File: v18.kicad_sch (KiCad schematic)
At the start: 59 parts, among them U51 ADP5071ACPZ, U52 TPS7A4700xRGW, U53 TPS7A3301RGW

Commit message: Whew.  DACs routed
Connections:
- net +20V: now also TP51.1
- net -20V: now also TP53.1
- net R18in: no longer TP51.1
- net RM18Vin: no longer TP53.1
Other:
- moved on the sheet: C523, C524, C525, C526, C527, C528, C529, C530, C543, C544, C545, C546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

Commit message: Tweaks following spice simulation.
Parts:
- added C551: 10u, Capacitor_SMD:C_0805_2012Metric, symbol Device:C
- added D55, D56: 1N5819WS, Diode_SMD:D_SOD-323, symbol Parts:1N5819WS
- added L56: 600, Inductor_SMD:L_0603_1608Metric, symbol Parts:L_Ferrite_Power
- L54, L55: value 100 -> 600; LCSC C14709 -> C1002
- renumbered C542 to C541, C543 to C542, C544 to C543, C545 to C544, C546 to C545, C547 to C546, C548 to C547, C549 to C548, C550 to C549, C551 to C550
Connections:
- net +18V: now also D55.1 (K)
- net -18V: now also C551.2, D56.2 (A), L56.2; no longer C544.2, C545.2, C546.2, C547.2, C548.2, C549.2, R541.1, TP54.1, U53.1 (OUT), U53.20 (OUT)
- net GNDPWR: now also C551.1, D55.2 (A), D56.1 (K)
- new net: C544.2, C545.2, C546.2, C547.2, C548.2, C549.2, L56.1, R541.1, TP54.1, U53.1 (OUT), U53.20 (OUT)
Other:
- moved on the sheet: C550

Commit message: About to delete scan...
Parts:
- C502: LCSC (none) -> C1588; now in the parts list
- D51, D52: Stock (none) -> 10
- L51, L52: Stock (none) -> 5
- R504: Stock (none) -> 50
- R513: Stock (none) -> 30
- TP51, TP52, TP53, TP54: Stock (none) -> -
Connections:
- net FB1: no longer names the net of R502.1, R503.2, R504.1, U51.5 (FB1)
- net FB2: no longer names the net of R512.2, R513.2, R514.1, U51.11 (FB2)
- net R18in: no longer names the net of C522.2, C523.2, R524.1, U52.13 (EN), U52.15 (IN), U52.16 (IN)
- net RM18Vin: no longer names the net of C541.1, C542.1, R544.1, U53.13 (EN), U53.15 (IN), U53.16 (IN)
- net Sn: no longer names the net of D52.1 (K), L52.1, U51.18 (SW2)
- net Sp: no longer names the net of D51.2 (A), L51.2, U51.20 (SW1)

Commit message: Scan deleted.
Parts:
- removed D53, D54: 1N5819WS, Diode_SMD:D_SOD-323, symbol Parts:1N5819WS
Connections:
- net at L54.2: now also R524.2
- net at L55.2: now also R544.2
- net +20V: no longer names the net of C504.2, C505.1, D51.1 (K), L54.1, R503.1, TP51.1
- net -20V: no longer names the net of C506.1, C508.2, D52.2 (A), L55.1, R514.2, TP53.1
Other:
- moved on the sheet: C522, C523, C524, C525, C526, C527, C528, C529, C530, C541, C542, C543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

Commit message: Most blocks there....
About to restore scan.
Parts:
- removed C550: 10u, Capacitor_SMD:C_0805_2012Metric, symbol Device:C
- removed R544: 1, Resistor_SMD:R_0603_1608Metric, symbol Device:R
- renumbered C507 to C50, C501 to C51, C504 to C52, C506 to C53
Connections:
- net -18V: now also C544.1, C545.1, C546.1, C547.1, C548.1, C549.1, R541.1, TP54.1, U53.1 (OUT), U53.20 (OUT); no longer C551.2, L56.2
- net GNDPWR: now also C52.2, C522.2, C523.2, C53.1, C543.2, C544.2, C546.2, C547.2, C548.2, C549.2, C551.2; no longer C52.1, C522.1, C523.1, C53.2, C543.1, C544.1, C546.1, C547.1, C548.1, C549.1, C551.1
- net at C505.1, D51.1 (K), L54.1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: now also C52.1; no longer C52.2
- net at C508.2, D52.2 (A), L55.1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: now also C53.2; no longer C53.1
- net i18: now reaches R524.1, U52.13 (EN), U52.15 (IN), U52.16 (IN)
- net i18: now also C522.1, C523.1; no longer C522.2, C523.2
- net at R541.2, R542.1, R543.1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: now also C545.2; no longer C545.1
- net im18: now reaches C541.1, C542.1, U53.13 (EN), U53.15 (IN), U53.16 (IN)
- net im18: now also L56.2
- net at L55.2: now also C551.1, L56.1
- net at U53.14 (NR/SS): now also C543.1; no longer C543.2
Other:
- moved on the sheet: C508, C52, C522, C523, C524, C525, C526, C527, C528, C529, C53, C530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

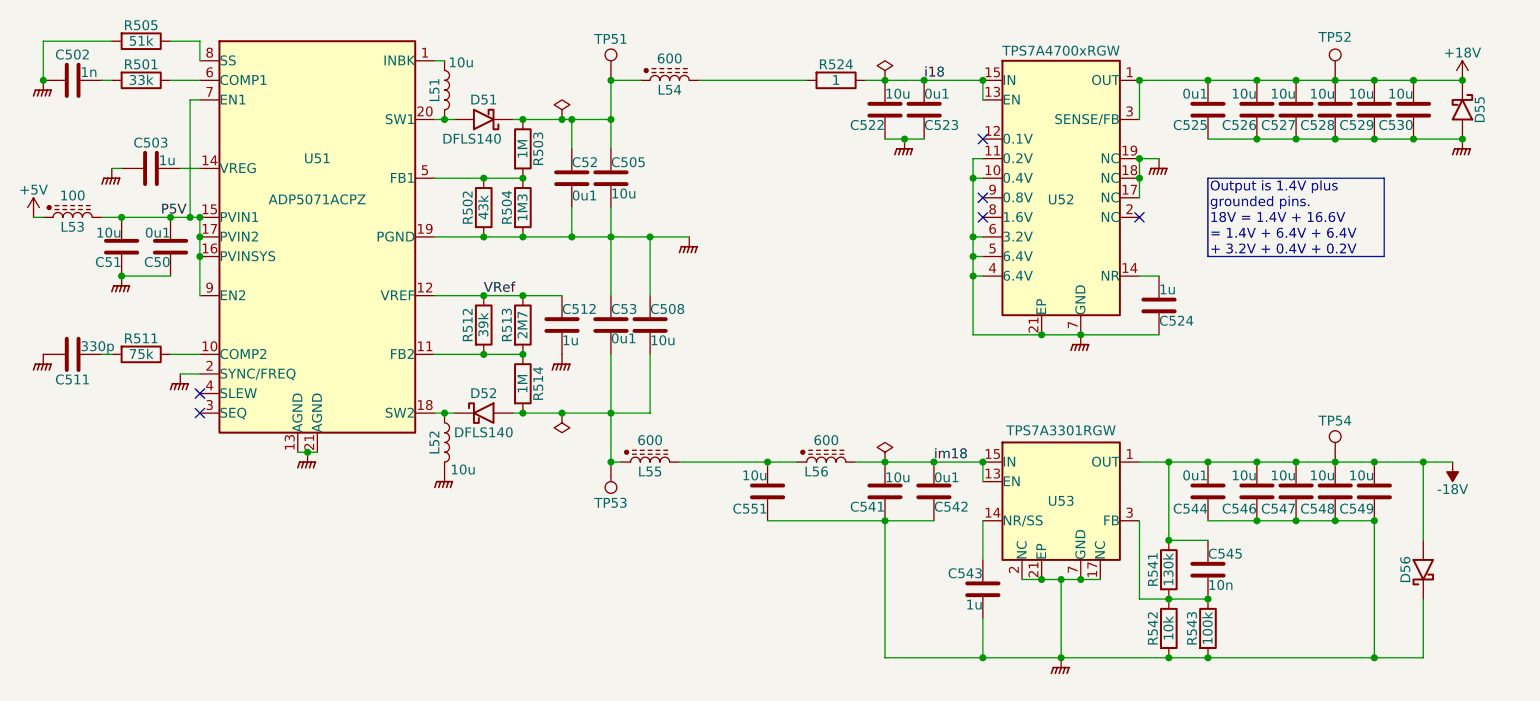
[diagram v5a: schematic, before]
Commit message: S&H restored.  Now to touch up connections etc.
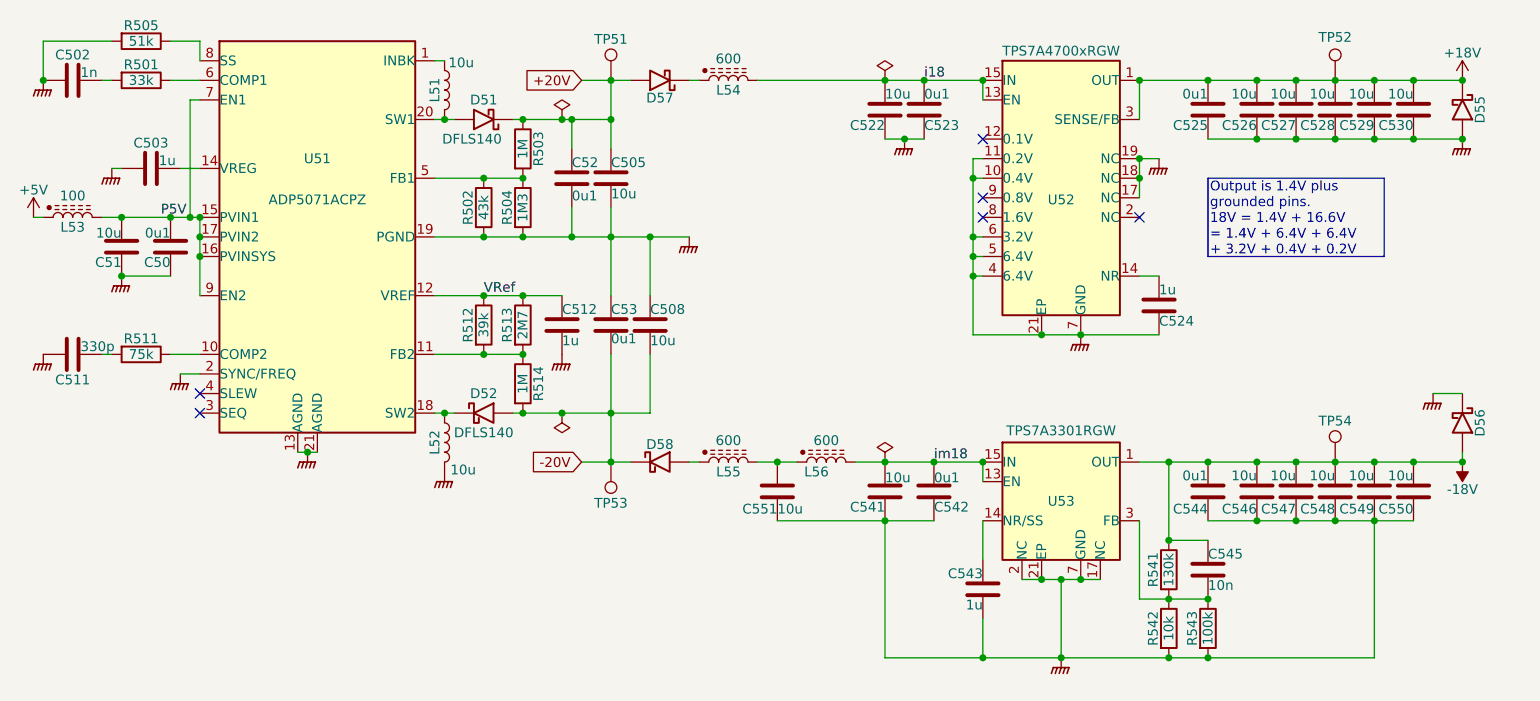
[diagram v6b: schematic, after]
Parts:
- removed R524: 1, Resistor_SMD:R_0603_1608Metric, symbol Device:R
- added C550: 10u, Capacitor_SMD:C_0805_2012Metric, symbol Device:C
- added D57, D58: 1N5819WS, Diode_SMD:D_SOD-323, symbol Parts:1N5819WS
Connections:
- net -18V: now also C550.1
- net GNDPWR: now also C550.2
- net i18: now also L54.2
- net +20V: now reaches C505.1, C52.1, D51.1 (K), R503.1, TP51.1
- net +20V: now also D57.2 (A); no longer L54.1
- net -20V: now reaches C508.2, C53.2, D52.2 (A), R514.2, TP53.1
- net -20V: now also D58.1 (K); no longer L55.1
- new net: D57.1 (K), L54.1
- new net: D58.2 (A), L55.1
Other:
- moved on the sheet: C551, D56, L54, L55

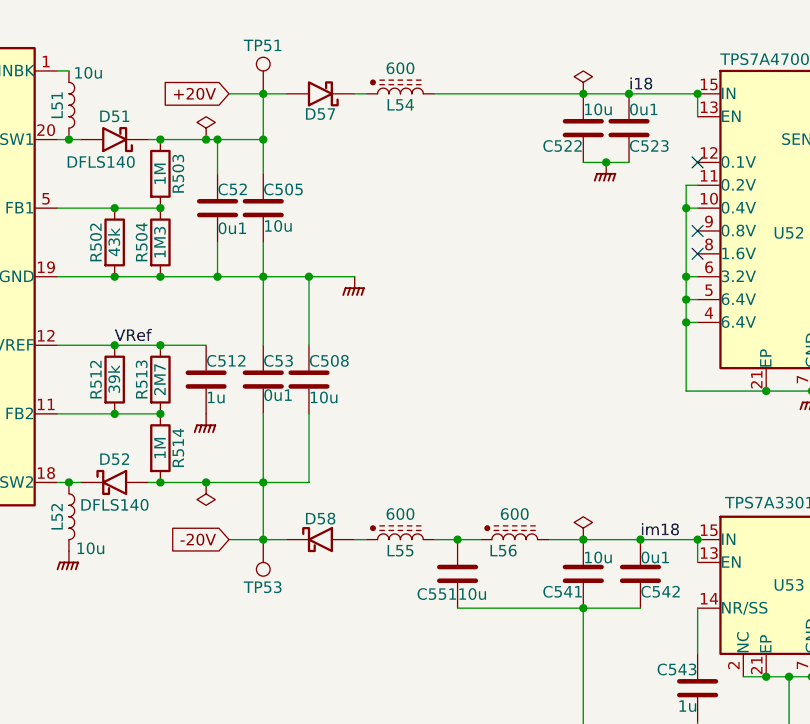
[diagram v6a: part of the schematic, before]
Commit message: Put ref filtering into the schematic.
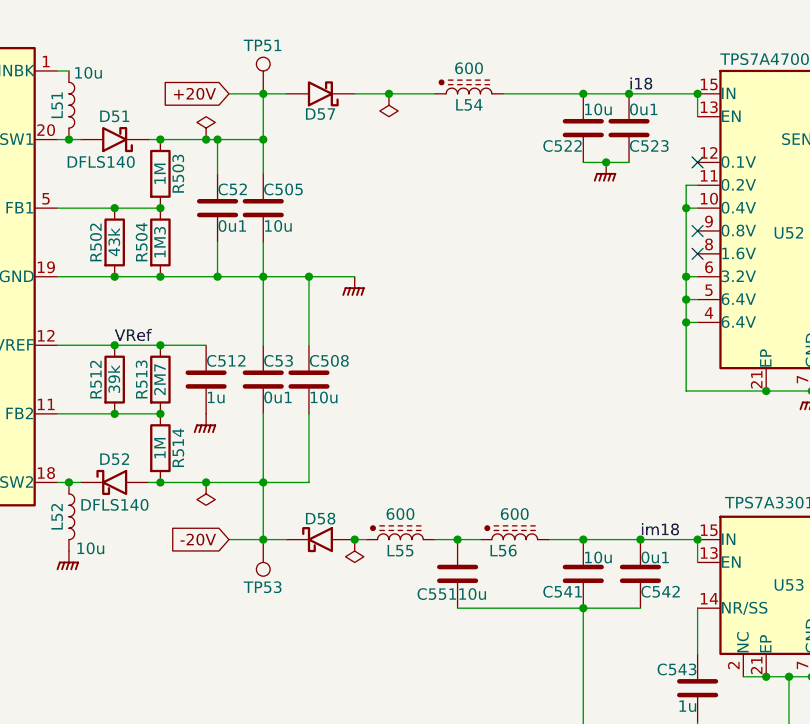
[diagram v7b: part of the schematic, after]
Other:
- moved on the sheet: L54
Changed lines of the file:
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@@
 	)
 	(junction
+		(at 144.78 92.71)
+		(diameter 0)
+		(color 0 0 0 0)
+	)
+	(junction
 		(at 245.11 50.8)
 		(diameter 0)
@@
 	)
 	(junction
+		(at 148.59 43.18)
+		(diameter 0)
+		(color 0 0 0 0)
+	)
+	(junction
 		(at 238.76 92.71)
 		(diameter 0)
@@
 	(wire
 		(pts
+			(xy 161.29 43.18) (xy 170.18 43.18)
+		)
+		(stroke
+			(width 0)
+			(type default)
+		)
+	)
+	(wire
+		(pts
 			(xy 134.62 52.07) (xy 134.62 48.26)
 		)
@@
 	(wire
 		(pts
-			(xy 144.78 43.18) (xy 146.05 43.18)
-		)
-		(stroke
-			(width 0)
-			(type default)
-		)
-	)
-	(wire
-		(pts
 			(xy 81.28 66.04) (xy 81.28 71.12)
 		)
@@
 	(wire
 		(pts
-			(xy 71.12 60.96) (xy 77.47 60.96)
+			(xy 144.78 43.18) (xy 148.59 43.18)
 		)
 		(stroke
@@
 	(wire
 		(pts
-			(xy 111.76 55.88) (xy 118.11 55.88)
+			(xy 71.12 60.96) (xy 77.47 60.96)
 		)
 		(stroke
@@
 	(wire
 		(pts
-			(xy 203.2 55.88) (xy 203.2 58.42)
+			(xy 111.76 55.88) (xy 118.11 55.88)
 		)
 		(stroke
@@
 	(wire
 		(pts
-			(xy 170.18 43.18) (xy 175.26 43.18)
+			(xy 203.2 55.88) (xy 203.2 58.42)
 		)
 		(stroke
@@
 	(wire
 		(pts
-			(xy 223.52 100.33) (xy 228.6 100.33)
+			(xy 170.18 43.18) (xy 175.26 43.18)
 		)
 		(stroke
@@
 	(wire
 		(pts
-			(xy 153.67 43.18) (xy 170.18 43.18)
+			(xy 223.52 100.33) (xy 228.6 100.33)
 		)
 		(stroke
@@
 	(wire
 		(pts
+			(xy 148.59 43.18) (xy 153.67 43.18)
+		)
+		(stroke
+			(width 0)
+			(type default)
+		)
+	)
+	(wire
+		(pts
 			(xy 144.78 92.71) (xy 146.05 92.71)
 		)
@@
 	(symbol
 		(lib_id "Parts:L_Ferrite_Power")
-		(at 149.86 43.18 90)
+		(at 157.48 43.18 90)
 		(unit 1)
 		(exclude_from_sim no)
@@
 		(dnp no)
 		(property "Reference" "L54"
-			(at 149.86 44.45 90)
+			(at 157.48 44.45 90)
 			(effects
 				(font
@@
 		)
 		(property "Value" "600"
-			(at 149.86 40.386 90)
+			(at 157.48 40.386 90)
 			(effects
 				(font
@@
 		)
 		(property "Footprint" "Inductor_SMD:L_0603_1608Metric"
-			(at 149.86 43.18 0)
+			(at 157.48 43.18 0)
 			(effects
 				(font
@@
 		)
 		(property "Datasheet" "200mA / 450mΩ"
-			(at 149.86 43.18 0)
+			(at 157.48 43.18 0)
 			(effects
 				(font
@@
 		)
 		(property "Description" "Inductor with ferrite core"
-			(at 149.86 43.18 0)
+			(at 157.48 43.18 0)
 			(effects
 				(font
@@
 		)
 		(property "LCSC" "C1002"
-			(at 149.86 43.18 90)
+			(at 157.48 43.18 90)
 			(effects
 				(font
@@
 		)
 		(property "Stock" ""
-			(at 149.86 43.18 90)
+			(at 157.48 43.18 90)
 			(effects
 				(font
@@
 		)
 		(property "Value" "0u1"
-			(at 129.54 58.166 0)
+			(at 129.54 57.912 0)
 			(effects
 				(font
@@
 	(symbol
 		(lib_id "power:PWR_FLAG")
-		(at 170.18 92.71 0)
+		(at 144.78 92.71 180)
 		(unit 1)
 		(exclude_from_sim no)
@@
 		(dnp no)
 		(property "Reference" "#FLG0101"
-			(at 170.18 90.805 0)
+			(at 144.78 94.615 0)
 			(effects
 				(font
@@
 		)
 		(property "Value" "PWR_FLAG"
-			(at 170.18 88.9 0)
+			(at 144.78 96.52 0)
 			(effects
 				(font
@@
 		)
 		(property "Footprint" ""
-			(at 170.18 92.71 0)
+			(at 144.78 92.71 0)
 			(effects
 				(font
@@
 		)
 		(property "Datasheet" "~"
-			(at 170.18 92.71 0)
+			(at 144.78 92.71 0)
 			(effects
 				(font
@@
 		)
 		(property "Description" "Special symbol for telling ERC where power comes from"
-			(at 170.18 92.71 0)
+			(at 144.78 92.71 0)
 			(effects
 				(font
@@
 		)
 		(property "Value" "0u1"
-			(at 134.62 76.708 0)
+			(at 134.62 76.962 0)
 			(effects
 				(font
@@
 	(symbol
 		(lib_id "power:PWR_FLAG")
-		(at 170.18 43.18 0)
+		(at 148.59 43.18 180)
 		(unit 1)
 		(exclude_from_sim no)
@@
 		(dnp no)
 		(property "Reference" "#FLG0102"
-			(at 170.18 41.275 0)
+			(at 148.59 45.085 0)
 			(effects
 				(font
@@
 		)
 		(property "Value" "PWR_FLAG"
-			(at 170.18 39.37 0)
+			(at 148.59 46.99 0)
 			(effects
 				(font
@@
 		)
 		(property "Footprint" ""
-			(at 170.18 43.18 0)
+			(at 148.59 43.18 0)
 			(effects
 				(font
@@
 		)
 		(property "Datasheet" "~"
-			(at 170.18 43.18 0)
+			(at 148.59 43.18 0)
 			(effects
 				(font
@@
 		)
 		(property "Description" "Special symbol for telling ERC where power comes from"
-			(at 170.18 43.18 0)
+			(at 148.59 43.18 0)
 			(effects
 				(font

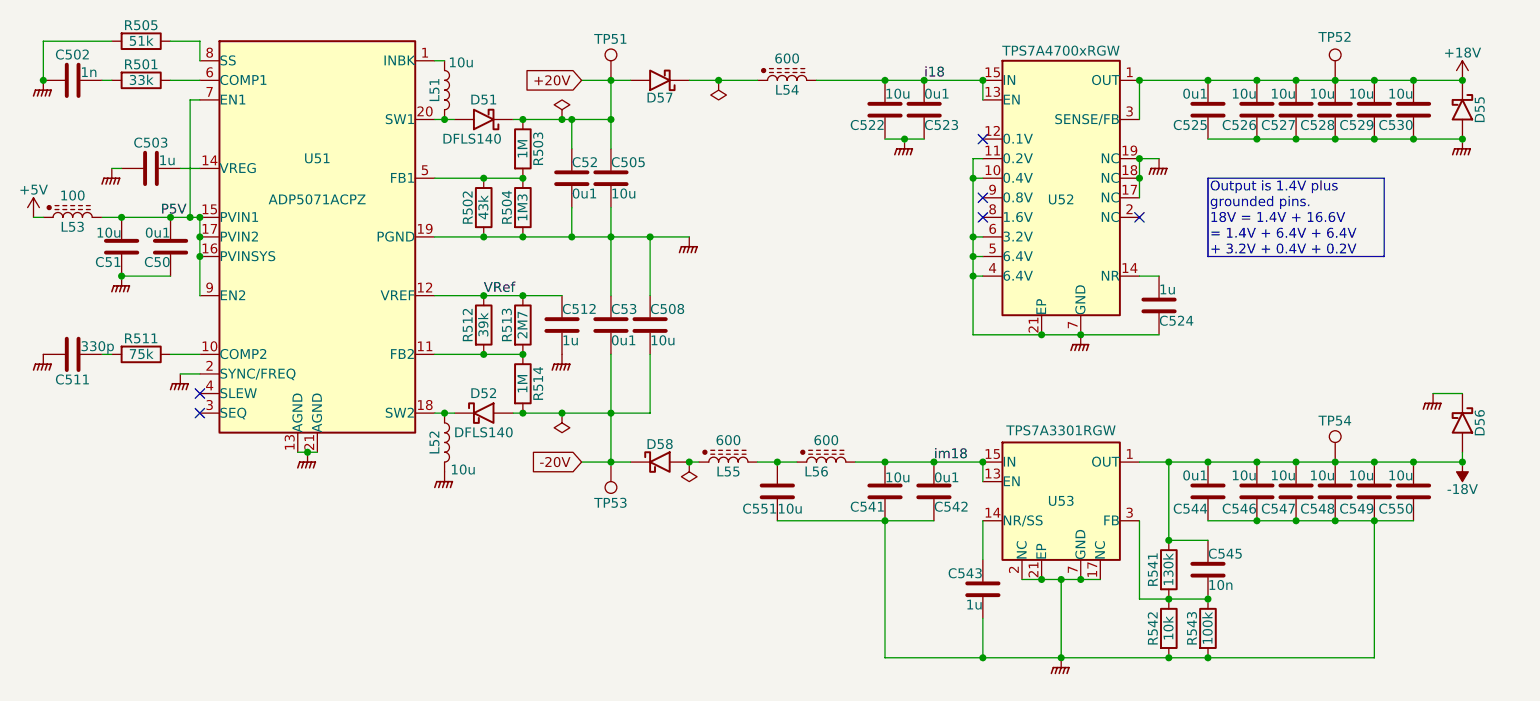
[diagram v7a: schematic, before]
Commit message: Adjust voltage rails.
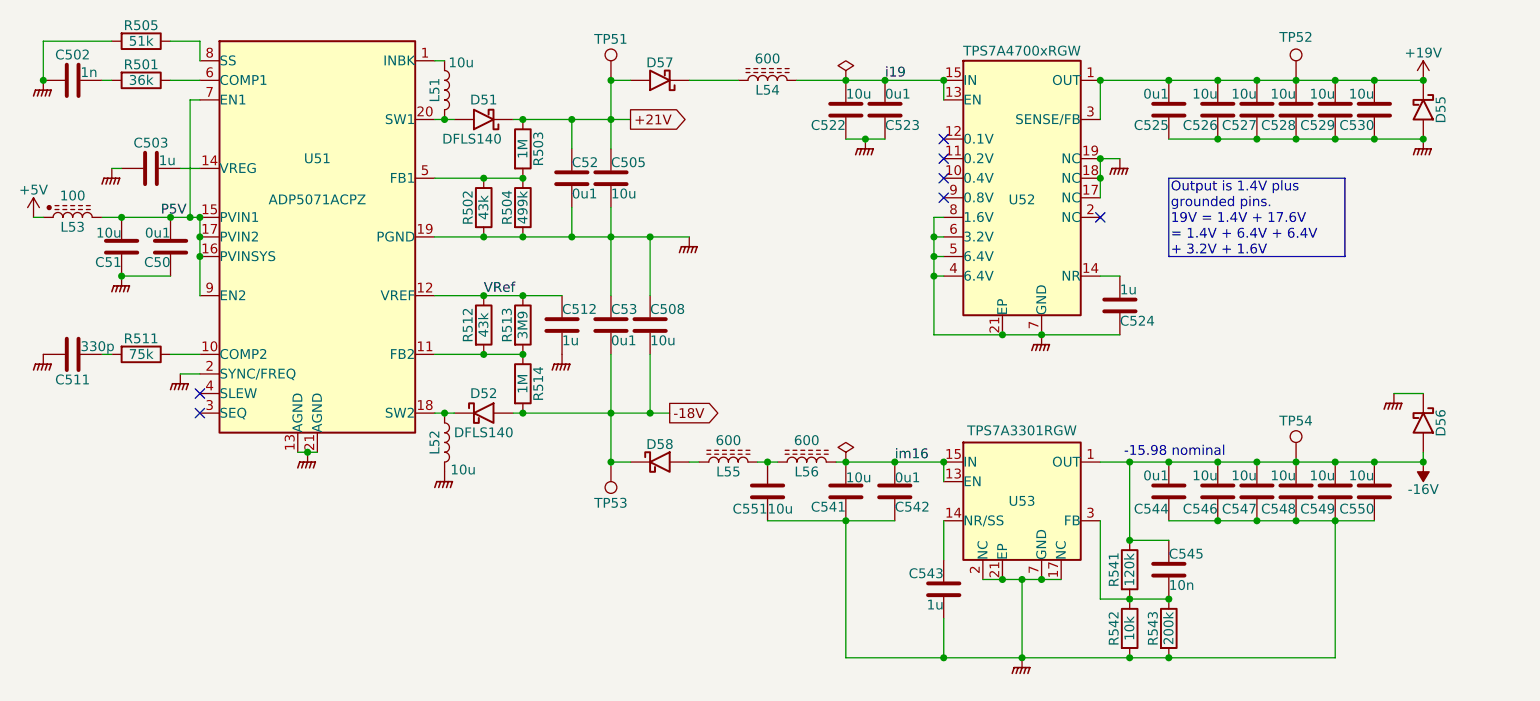
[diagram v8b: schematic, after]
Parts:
- D55, D56, D57, D58: footprint Diode_SMD:D_SOD-323 -> Parts:SOD-323
- L54, L55, L56: symbol Parts:L_Ferrite_Power -> Device:L_Ferrite
- R501: value 33k -> 36k; LCSC C4216 -> (none)
- R504: value 1M3 -> 499k
- R512: value 39k -> 43k; LCSC C23153 -> (none)
- R513: value 2M7 -> 3M9
- R541: value 130k -> 120k; LCSC C22795 -> (none)
- R543: value 100k -> 200k; footprint Resistor_SMD:R_0402_1005Metric -> Resistor_SMD:R_0603_1608Metric; LCSC C25741 -> C25811
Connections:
- net -20V is gone; now on net -18V: C508.2, C53.2, D52.2 (A), D58.1 (K), R514.2, TP53.1
- net -18V: no longer C544.1, C545.1, C546.1, C547.1, C548.1, C549.1, C550.1, D56.2 (A), R541.1, TP54.1, U53.1 (OUT), U53.20 (OUT)
- net GNDPWR: now also U52.8 (1.6V); no longer U52.10 (0.4V), U52.11 (0.2V)
- net +18V renamed +19V
- net +20V renamed +21V
- net i18 renamed i19
- net im18 renamed im16
- new net -16V: C544.1, C545.1, C546.1, C547.1, C548.1, C549.1, C550.1, D56.2 (A), R541.1, TP54.1, U53.1 (OUT), U53.20 (OUT)
- no-connect marks 6 -> 7
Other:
- note added: "-15.98 nominal"
- moved on the sheet: C522, C523, C524, C525, C526, C527, C528, C529, C530, C541, C542, C543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
